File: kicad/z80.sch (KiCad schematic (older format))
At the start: 17 parts, among them U1 Z80CPU, U2 z80pcb

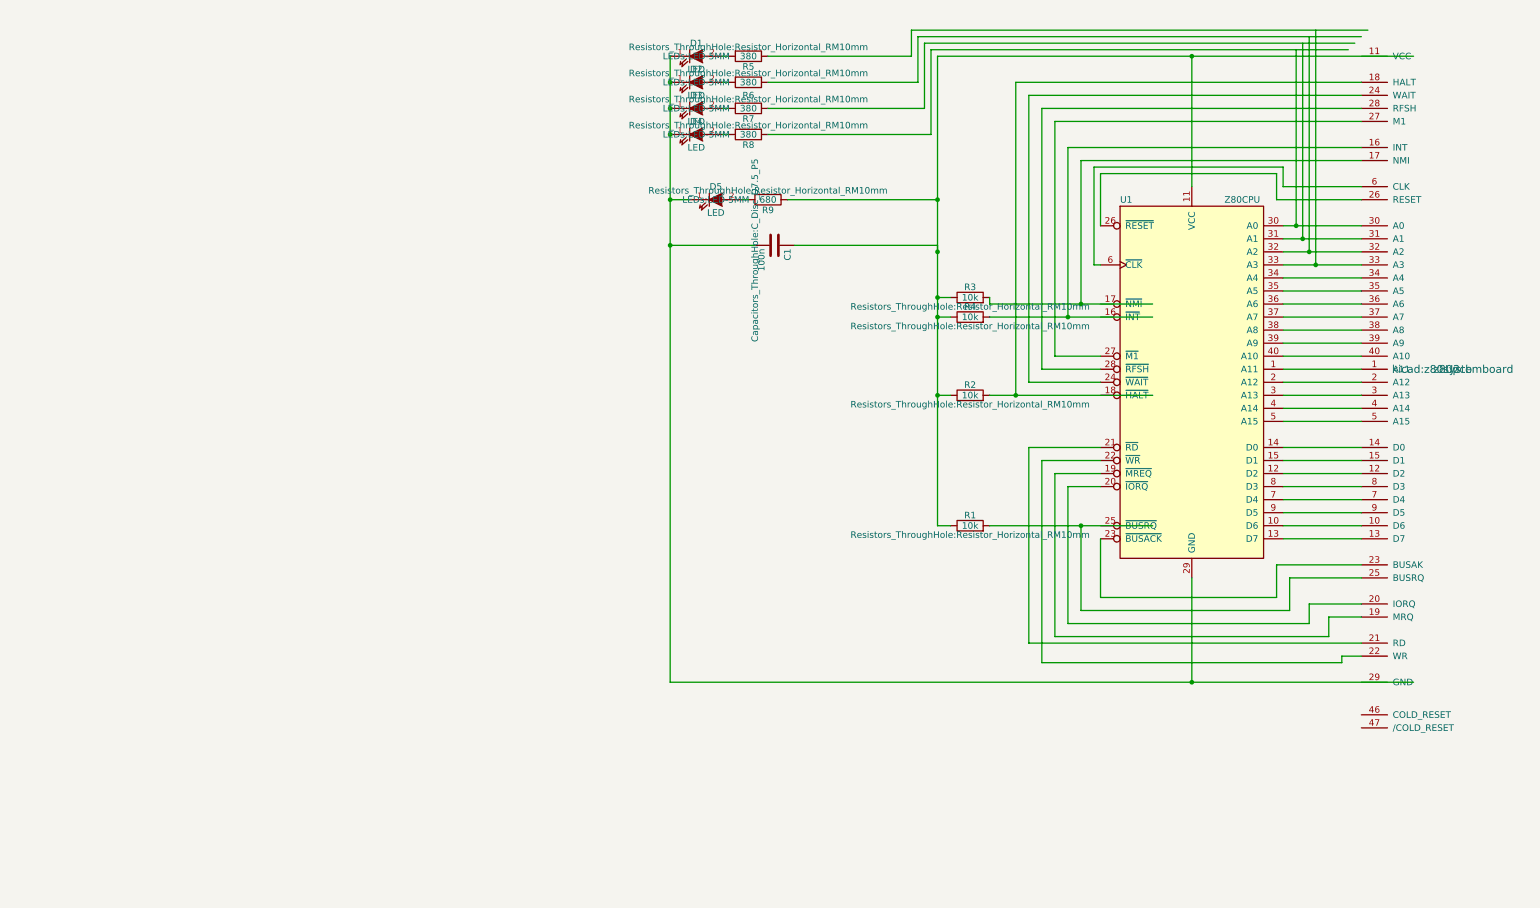
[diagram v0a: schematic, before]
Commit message: add reset circuit
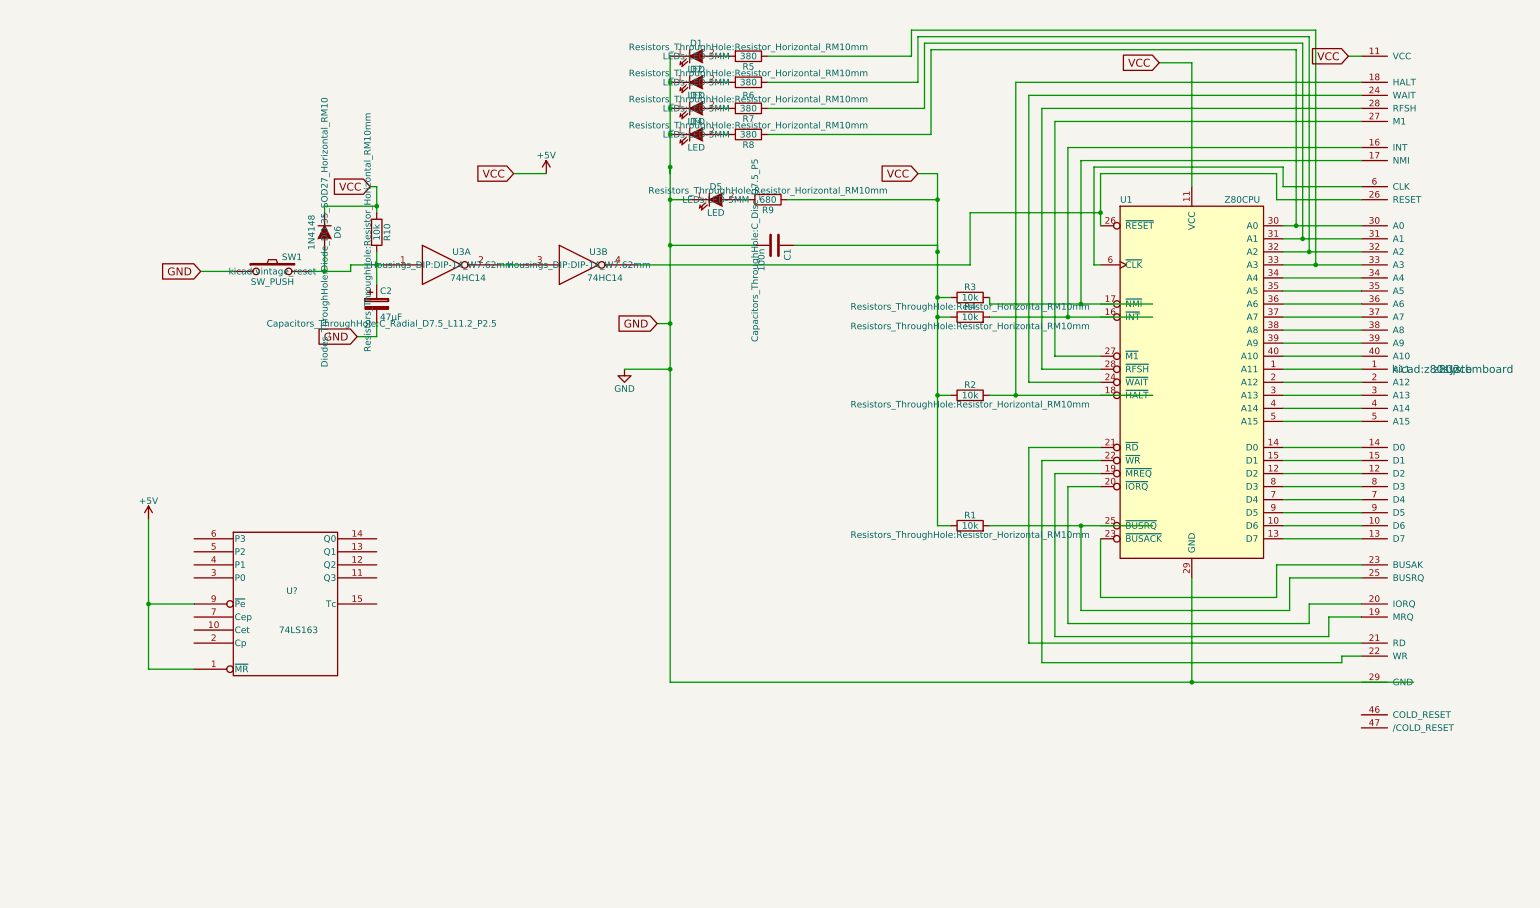
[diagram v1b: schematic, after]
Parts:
- added C2: 47μF, Capacitors_ThroughHole:C_Radial_D7.5_L11.2_P2.5, symbol CP
- added D6: 1N4148, Diodes_ThroughHole:Diode_DO-35_SOD27_Horizontal_RM10, symbol D
- added R10: 10k, Resistors_ThroughHole:Resistor_Horizontal_RM10mm, symbol R
- added SW1: SW_PUSH, kicad:vintage_reset, symbol SW_PUSH
- added U3: 74HC14, Housings_DIP:DIP-14_W7.62mm, symbol 74HC14
- added U?: 74LS163, symbol 74LS163
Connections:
- net labels added: +5V, GND, VCC
- wire segments 115 -> 140
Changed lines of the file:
@@
 	0    1    1    0
 $EndComp
+$Comp
+L 74HC14 U3
+U 2 1 57281A52
+P 4700 2400
+F 0 "U3" H 4850 2500 50  0000 C CNN
+F 1 "74HC14" H 4900 2300 50  0000 C CNN
+F 2 "Housings_DIP:DIP-14_W7.62mm" H 4700 2400 50  0000 C CNN
+F 3 "" H 4700 2400 50  0000 C CNN
+	2    4700 2400
+	1    0    0    -1
+$EndComp
+Text GLabel 5300 2850 0    60   Input ~ 0
+GND
+Text GLabel 10600 800  0    60   Input ~ 0
+VCC
+Text GLabel 9150 850  0    60   Input ~ 0
+VCC
+Text GLabel 7300 1700 0    60   Input ~ 0
+VCC
+$Comp
+L 74HC14 U3
+U 1 1 57285E4E
+P 3650 2400
+F 0 "U3" H 3800 2500 50  0000 C CNN
+F 1 "74HC14" H 3850 2300 50  0000 C CNN
+F 2 "Housings_DIP:DIP-14_W7.62mm" H 3650 2400 50  0000 C CNN
+F 3 "" H 3650 2400 50  0000 C CNN
+	1    3650 2400
+	1    0    0    -1
+$EndComp
+$Comp
+L R R10
+U 1 1 57285F93
+P 3150 2150
+F 0 "R10" V 3230 2150 50  0000 C CNN
+F 1 "10k" V 3150 2150 50  0000 C CNN
+F 2 "Resistors_ThroughHole:Resistor_Horizontal_RM10mm" V 3080 2150 50  0000 C CNN
+F 3 "" H 3150 2150 50  0000 C CNN
+	1    3150 2150
+	1    0    0    -1
+$EndComp
+$Comp
+L SW_PUSH SW1
+U 1 1 57285FF0
+P 2350 2450
+F 0 "SW1" H 2500 2560 50  0000 C CNN
+F 1 "SW_PUSH" H 2350 2370 50  0000 C CNN
+F 2 "kicad:vintage_reset" H 2350 2450 50  0000 C CNN
+F 3 "" H 2350 2450 50  0000 C CNN
+	1    2350 2450
+	1    0    0    -1
+$EndComp
+$Comp
+L CP C2
+U 1 1 572860AB
+P 3150 2700
+F 0 "C2" H 3175 2800 50  0000 L CNN
+F 1 "47μF" H 3175 2600 50  0000 L CNN
+F 2 "Capacitors_ThroughHole:C_Radial_D7.5_L11.2_P2.5" H 3188 2550 50  0000 C CNN
+F 3 "" H 3150 2700 50  0000 C CNN
+	1    3150 2700
+	1    0    0    -1
+$EndComp
+$Comp
+L D D6
+U 1 1 57286136
+P 2750 2150
+F 0 "D6" H 2750 2250 50  0000 C CNN
+F 1 "1N4148" H 2750 2050 50  0000 C CNN
+F 2 "Diodes_ThroughHole:Diode_DO-35_SOD27_Horizontal_RM10" H 2750 2150 50  0000 C CNN
+F 3 "" H 2750 2150 50  0000 C CNN
+	1    2750 2150
+	0    1    1    0
+$EndComp
 Wire Wire Line
 	10100 2100 10700 2100
 Wire Wire Line
 	10100 2200 10700 2200
-Wire Wire Line
-	10100 2300 10700 2300
 Wire Wire Line
 	10100 2400 10700 2400
@@
 	7450 4400 7550 4400
 Wire Wire Line
-	7450 800  7450 4400
+	7450 1700 7450 4400
 Wire Wire Line
 	8700 4100 8450 4100
@@
 Connection ~ 7450 2800
 Wire Wire Line
-	8700 2100 8700 1700
+	8700 1700 8700 2100
 Wire Wire Line
 	8700 1700 10050 1700
@@
 Connection ~ 8550 2700
 Wire Wire Line
-	7450 800  11100 800
-Wire Wire Line
-	9400 1800 9400 800
-Connection ~ 9400 800
+	9150 850  9400 850
+Wire Wire Line
+	9400 850  9400 1800
 Wire Wire Line
 	8450 2800 8450 1500
@@
 	10200 2100 10200 750
 Wire Wire Line
-	10600 750  7400 750
+	10200 750  7400 750
 Wire Wire Line
 	7400 750  7400 1400
@@
 Connection ~ 10200 2100
 Wire Wire Line
-	10250 2200 10250 700
-Wire Wire Line
-	10650 700  7350 700
+	7300 650  10300 650
 Wire Wire Line
 	7350 700  7350 1200
@@
 Connection ~ 10250 2200
 Wire Wire Line
-	10300 2300 10300 650
-Wire Wire Line
-	10700 650  7300 650
-Wire Wire Line
 	7300 650  7300 1000
 Wire Wire Line
 	7300 1000 6150 1000
-Connection ~ 10300 2300
-Wire Wire Line
-	10350 2400 10350 600
-Wire Wire Line
-	10750 600  7250 600
+Wire Wire Line
+	10350 600  7250 600
 Wire Wire Line
 	7250 600  7250 800
@@
 	7450 2250 7450 2300
 Connection ~ 7450 2300
+Wire Wire Line
+	7700 2000 8700 2000
+Wire Wire Line
+	7700 2400 7700 2000
+Connection ~ 8700 2000
+Wire Wire Line
+	5150 2400 7700 2400
+Wire Wire Line
+	4100 2400 4250 2400
+Wire Wire Line
+	5300 2850 5400 2850
+Connection ~ 5400 2850
+Wire Wire Line
+	10600 800  10700 800
+Wire Wire Line
+	7350 700  10250 700
+Wire Wire Line
+	10250 700  10250 2200
+Wire Wire Line
+	10100 2300 10700 2300
+Wire Wire Line
+	10300 650  10300 2300
+Connection ~ 10300 2300
+Wire Wire Line
+	10350 600  10350 2400
+Wire Wire Line
+	7300 1700 7450 1700
+Wire Wire Line
+	3150 2300 3150 2550
+Wire Wire Line
+	2950 2400 3200 2400
+Text GLabel 3100 1800 0    60   Input ~ 0
+VCC
+Wire Wire Line
+	3100 1800 3150 1800
+Wire Wire Line
+	3150 1800 3150 2000
+Text GLabel 3000 2950 0    60   Input ~ 0
+GND
+Wire Wire Line
+	3000 2950 3150 2950
+Wire Wire Line
+	3150 2950 3150 2850
+Connection ~ 3150 2400
+Text GLabel 1800 2450 0    60   Input ~ 0
+GND
+Wire Wire Line
+	1800 2450 2050 2450
+Wire Wire Line
+	2750 2000 2750 1950
+Wire Wire Line
+	2750 1950 3150 1950
+Connection ~ 3150 1950
+Wire Wire Line
+	2750 2300 2750 2450
+Wire Wire Line
+	2650 2450 2950 2450
+Wire Wire Line
+	2950 2450 2950 2400
+Connection ~ 2750 2450
+$Comp
+L +5V #PWR01
+U 1 1 5728826A
+P 4450 1700
+F 0 "#PWR01" H 4450 1550 50  0001 C CNN
+F 1 "+5V" H 4450 1840 50  0000 C CNN
+F 2 "" H 4450 1700 50  0000 C CNN
+F 3 "" H 4450 1700 50  0000 C CNN
+	1    4450 1700
+	1    0    0    -1
+$EndComp
+Wire Wire Line
+	5400 1700 5400 1650
+Connection ~ 5400 1650
+Text GLabel 4200 1700 0    60   Input ~ 0
+VCC
+Wire Wire Line
+	4200 1700 4450 1700
+$Comp
+L GND #PWR02
+U 1 1 572887E4
+P 5050 3200
+F 0 "#PWR02" H 5050 2950 50  0001 C CNN
+F 1 "GND" H 5050 3050 50  0000 C CNN
+F 2 "" H 5050 3200 50  0000 C CNN
+F 3 "" H 5050 3200 50  0000 C CNN
+	1    5050 3200
+	1    0    0    -1
+$EndComp
+Wire Wire Line
+	5050 3200 5400 3200
+Connection ~ 5400 3200
+$Comp
+L 74LS163 U?
+U 1 1 5728B2B4
+P 2450 5000
+F 0 "U?" H 2500 5100 50  0000 C CNN
+F 1 "74LS163" H 2550 4800 50  0000 C CNN
+F 2 "" H 2450 5000 50  0000 C CNN
+F 3 "" H 2450 5000 50  0000 C CNN
+	1    2450 5000
+	1    0    0    -1
+$EndComp
+$Comp
+L +5V #PWR?
+U 1 1 5728BB0F
+P 1400 4350
+F 0 "#PWR?" H 1400 4200 50  0001 C CNN
+F 1 "+5V" H 1400 4490 50  0000 C CNN
+F 2 "" H 1400 4350 50  0000 C CNN
+F 3 "" H 1400 4350 50  0000 C CNN
+	1    1400 4350
+	1    0    0    -1
+$EndComp
+Wire Wire Line
+	1400 4350 1400 5500
+Wire Wire Line
+	1400 5500 1750 5500
+Wire Wire Line
+	1750 5000 1400 5000
+Connection ~ 1400 5000
 $EndSCHEMATC

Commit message: fixed connections
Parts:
- U4: renamed from U?; footprint (none) -> Housings_DIP:DIP-16_W7.62mm
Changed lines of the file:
@@
 	10050 4700 10700 4700
 Wire Wire Line
-	7850 4400 9100 4400
+	7850 4400 8700 4400
 Wire Wire Line
 	8550 4400 8550 5050
@@
 	9400 4800 9400 5600
 Wire Wire Line
-	5400 5600 11100 5600
+	5400 5600 10700 5600
 Wire Wire Line
 	7550 3400 7450 3400
 Connection ~ 7450 3400
 Wire Wire Line
-	7850 3400 9100 3400
-Wire Wire Line
-	7850 2800 9100 2800
-Wire Wire Line
-	7850 2700 9100 2700
+	7850 2800 8700 2800
 Wire Wire Line
 	7850 2700 7850 2650
@@
 Connection ~ 5400 3200
 $Comp
-L 74LS163 U?
+L 74LS163 U4
 U 1 1 5728B2B4
 P 2450 5000
-F 0 "U?" H 2500 5100 50  0000 C CNN
+F 0 "U4" H 2500 5100 50  0000 C CNN
 F 1 "74LS163" H 2550 4800 50  0000 C CNN
-F 2 "" H 2450 5000 50  0000 C CNN
+F 2 "Housings_DIP:DIP-16_W7.62mm" H 2450 5000 50  0000 C CNN
 F 3 "" H 2450 5000 50  0000 C CNN
 	1    2450 5000
@@
 $EndComp
 $Comp
-L +5V #PWR?
+L +5V #PWR03
 U 1 1 5728BB0F
 P 1400 4350
-F 0 "#PWR?" H 1400 4200 50  0001 C CNN
+F 0 "#PWR03" H 1400 4200 50  0001 C CNN
 F 1 "+5V" H 1400 4490 50  0000 C CNN
 F 2 "" H 1400 4350 50  0000 C CNN
@@
 	1750 5000 1400 5000
 Connection ~ 1400 5000
+Wire Wire Line
+	7850 3400 8700 3400
+Wire Wire Line
+	7850 2700 8700 2700
 $EndSCHEMATC

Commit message: finish cpu board draft
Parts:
- removed U3: 74HC14, Housings_DIP:DIP-14_W7.62mm, symbol 74HC14
- added C3: 10μF, Capacitors_ThroughHole:C_Radial_D7.5_L11.2_P2.5, symbol CP
- added D7: 1N4148, Diodes_ThroughHole:Diode_DO-35_SOD27_Horizontal_RM10, symbol D
- added P1: USB_B, Connect:USB_B, symbol USB_B
- added R11: 10k, Resistors_ThroughHole:Resistor_Horizontal_RM10mm, symbol R
- added SW2: SW_PUSH, kicad:vintage_reset, symbol SW_PUSH
- added U3: 74LS132, Housings_DIP:DIP-14_W7.62mm, symbol 74LS132
- added X1: 16.000Mhz, Oscillators:KXO-200_LargePads, symbol XO-14S
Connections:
- net +5V: now also U4.10 (Cet), U4.7 (Cep), D7.1 (K), P1.1 (VCC), R11.1, U3.14 (VCC), U3.14 (VCC), U3.14 (VCC), U3.14 (VCC), X1.14 (VCC)
- net GND: now also U4.3 (P0), U4.4 (P1), U4.5 (P2), U4.6 (P3), C3.2, P1.4 (GND), SW2.1, U3.7 (GND), U3.7 (GND), U3.7 (GND), U3.7 (GND), X1.7 (GND)
- net at U1.26 (~RESET~), U2.26 (RESET): now also U3.6
- net CLOCK: now reaches U1.6 (~CLK~), U2.6 (CLK)
- net CLOCK: now also U4.13 (Q1)
- net at U2.46 (COLD_RESET): now also U3.8
- net at U2.47 (/COLD_RESET): now also U3.10, U3.11, U3.9
- net at C2.1, D6.2 (A), R10.2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: now also U3.1
- net at U4.2 (Cp): now also X1.8 (OUT)
- new net: C3.1, D7.2 (A), R11.2, SW2.2, U3.12, U3.13, U3.2
- new net: U3.3, U3.4, U3.5
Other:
- moved on the sheet: C1, C2, D1, D2, D3, D4, D5, D6, R10, R5, R6, R7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
